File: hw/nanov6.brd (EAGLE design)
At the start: 34.9 x 35.2 mm, 28 parts, among them CON1 503548-1220, J1 M08X2, Q4 BSS138, U1 TPS622XX

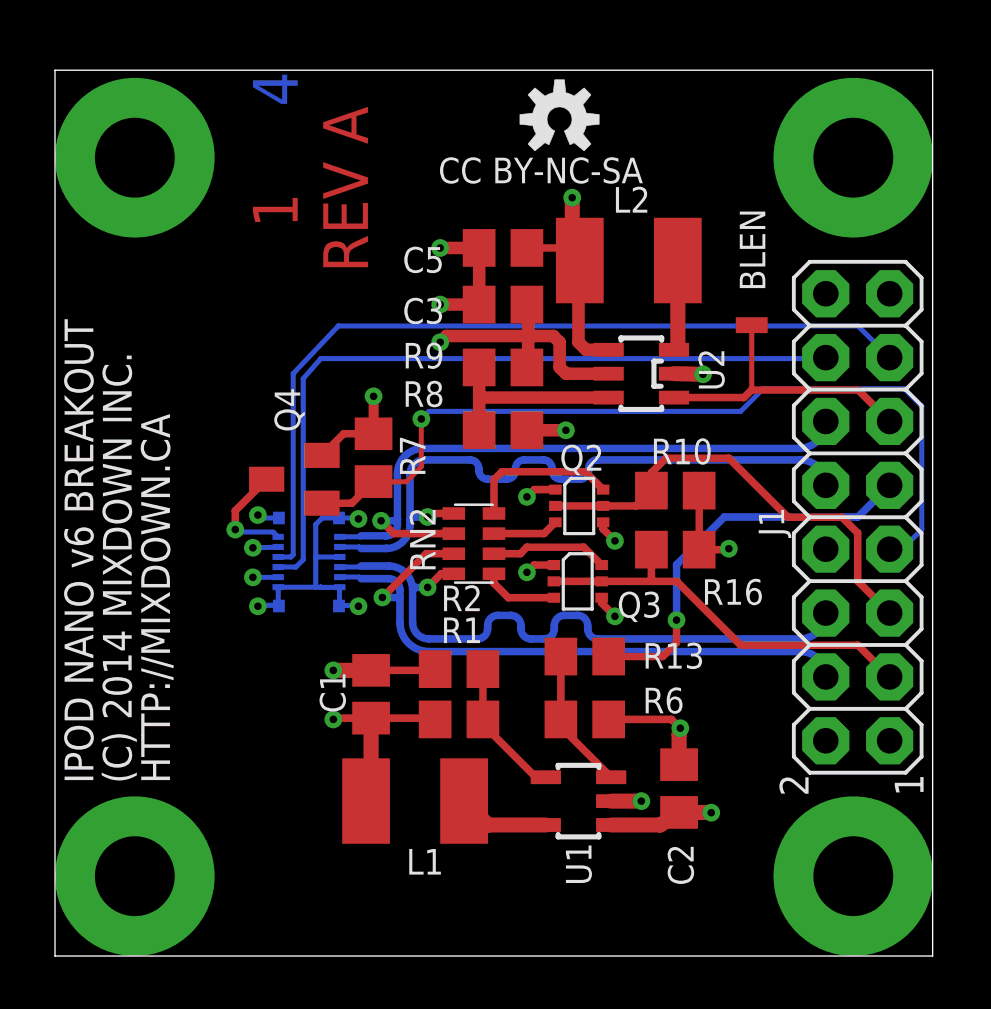
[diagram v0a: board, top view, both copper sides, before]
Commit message: add pulldown to RST#, make 3.3VEN active-high. Resolves #471, refs #469.
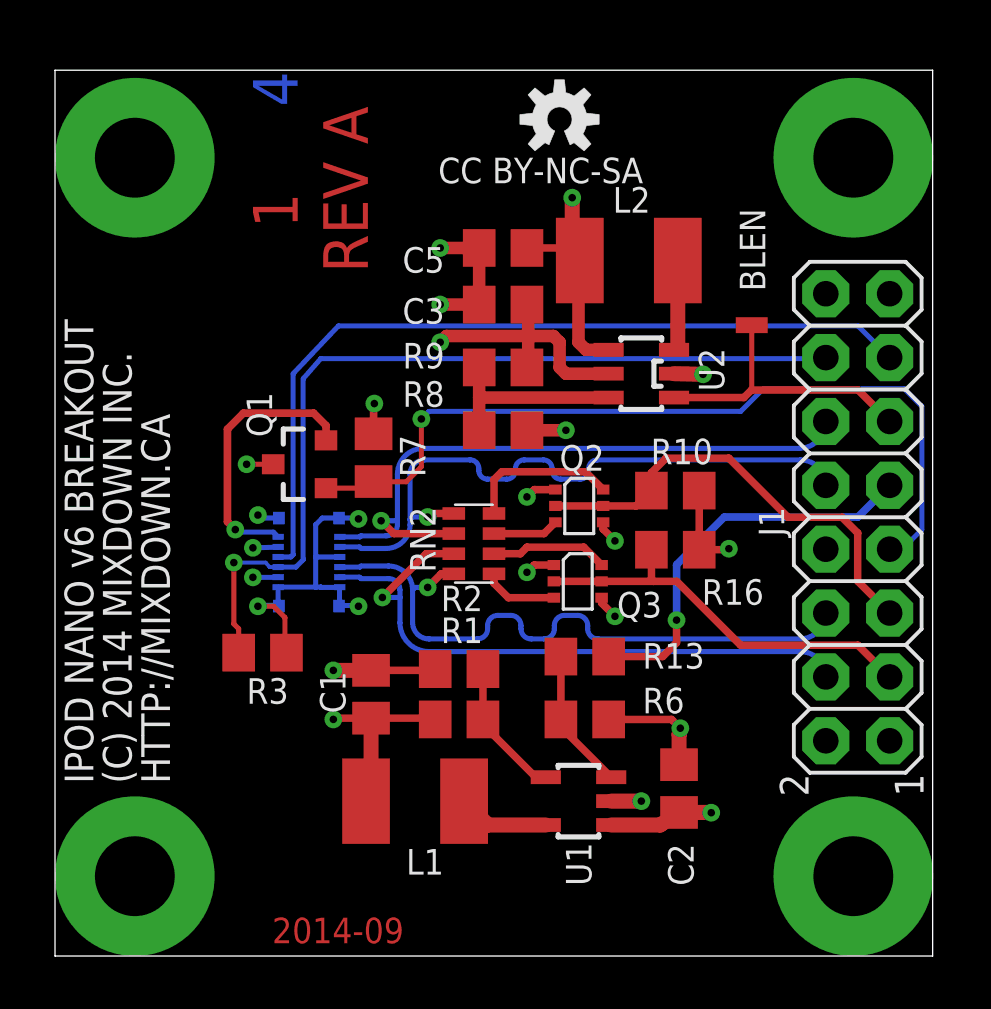
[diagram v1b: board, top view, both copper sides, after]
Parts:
- removed Q4: BSS138, SparkFun:SOT23
- added Q1: BSS84, SparkFun:SOT23-3
- added R3: 1k, rcl:R0805
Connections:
- net +3.3: now also Q1.3; no longer Q4.2, R7.2
- net 3.3VEN: now also Q1.1; no longer Q4.1
- net 3.3_SW: now also Q1.2; no longer Q4.3
- net GND: now also R3.2, R7.2
- net RST#: now also R3.1
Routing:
- net 3.3_SW: track 4.34 -> 10.9 mm
- net RST#: track 29.5 -> 35.0 mm, vias 0 -> 1
- net GND: track 37.4 -> 41.3 mm, vias 16 -> 17
- net +3.3: track 19.1 -> 16.2 mm
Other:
- board text added: "2014-09"

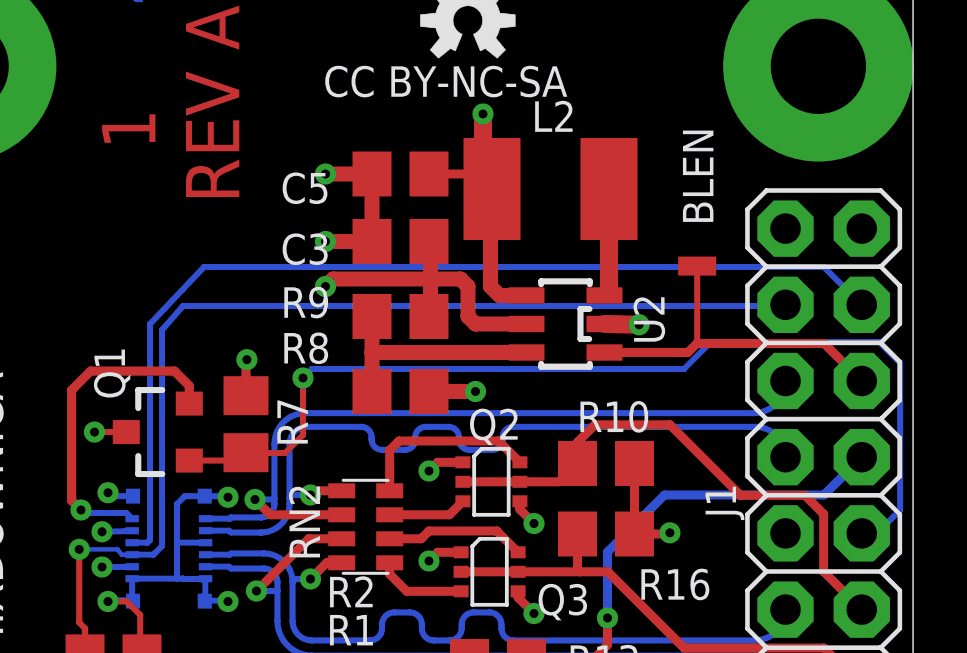
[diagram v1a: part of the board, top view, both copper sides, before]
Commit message: add pulldown to BLEN. Resolves #469.
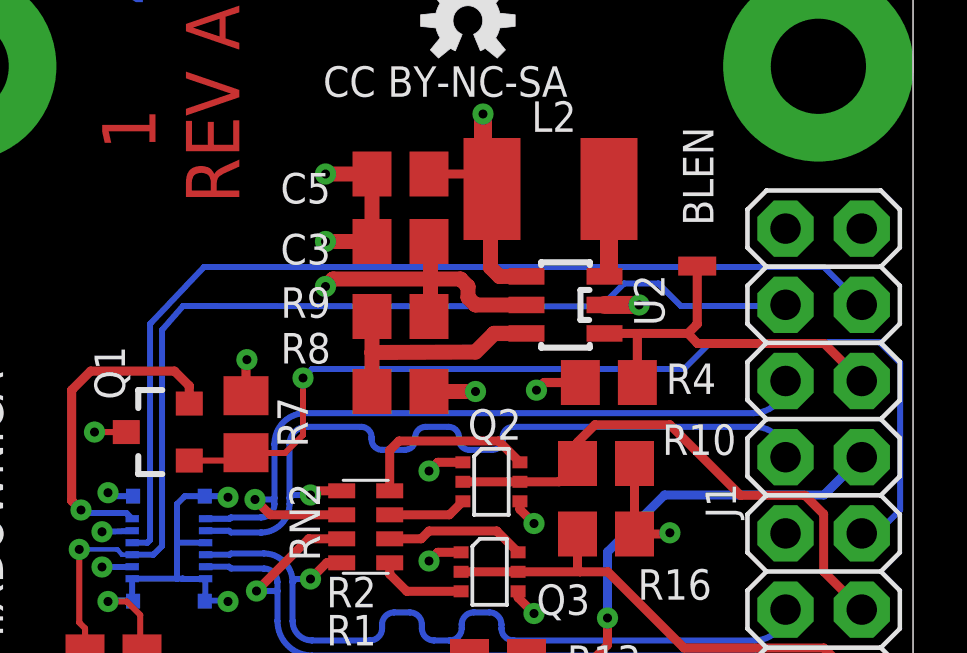
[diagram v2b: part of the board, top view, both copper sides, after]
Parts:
- added R4: 1k, rcl:R0805
- moved U2 0.64 mm to (23.3, 23.8)
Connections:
- net BL: now also R4.1
- net GND: now also R4.2
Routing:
- net GND: track 41.3 -> 42.9 mm, vias 17 -> 18
- net BL: track 11.8 -> 13.3 mm
- net N$7: track 3.61 -> 2.98 mm
- net LED+: track 26.3 -> 25.7 mm
- net +3.3: track 16.2 -> 15.6 mm
- net RST#: track 35.0 -> 35.6 mm
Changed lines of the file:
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@@
 <setting verticaltext="up"/>
 </settings>
-<grid distance="25" unitdist="mil" unit="mil" style="lines" multiple="1" display="yes" altdistance="0.025" altunitdist="inch" altunit="inch"/>
+<grid distance="5" unitdist="mil" unit="mil" style="lines" multiple="1" display="yes" altdistance="0.025" altunitdist="inch" altunit="inch"/>
 <layers>
 <layer number="1" name="Top" color="4" fill="1" visible="yes" active="yes"/>
@@
 <layer number="37" name="tTest" color="7" fill="1" visible="no" active="yes"/>
 <layer number="38" name="bTest" color="7" fill="1" visible="no" active="yes"/>
-<layer number="39" name="tKeepout" color="4" fill="11" visible="no" active="yes"/>
+<layer number="39" name="tKeepout" color="4" fill="11" visible="yes" active="yes"/>
 <layer number="40" name="bKeepout" color="1" fill="11" visible="yes" active="yes"/>
 <layer number="41" name="tRestrict" color="4" fill="10" visible="yes" active="yes"/>
@@
 </element>
 <element name="R10" library="rcl" package="R0805" value="1k" x="24.67" y="18.51" smashed="yes" rot="R180">
-<attribute name="NAME" x="26.162" y="20.574" size="1.016" layer="25" ratio="10" rot="R180"/>
+<attribute name="NAME" x="26.543" y="18.796" size="1.016" layer="25" ratio="10"/>
 <attribute name="VALUE" x="25.305" y="21.05" size="1.27" layer="27" rot="R180"/>
 </element>
@@
 <attribute name="VALUE" x="15.21" y="19.185" size="1.27" layer="27" rot="R90"/>
 </element>
-<element name="U2" library="ak-misc" package="SOT23-6" value="" x="23.32" y="23.16" smashed="yes" rot="R90">
-<attribute name="NAME" x="26.622" y="22.4615" size="1.016" layer="25" ratio="10" rot="R90"/>
-<attribute name="VALUE" x="23.5105" y="22.2075" size="0.4064" layer="27" rot="R90"/>
+<element name="U2" library="ak-misc" package="SOT23-6" value="" x="23.32" y="23.795" smashed="yes" rot="R90">
+<attribute name="NAME" x="26.622" y="23.0965" size="1.016" layer="25" ratio="10" rot="R90"/>
+<attribute name="VALUE" x="23.5105" y="22.8425" size="0.4064" layer="27" rot="R90"/>
 </element>
 <element name="R8" library="rcl" package="R0805" value="TBD" x="17.82" y="20.91" smashed="yes">
@@
 <attribute name="NAME" x="7.62" y="10.033" size="1.016" layer="25" ratio="10"/>
 <attribute name="VALUE" x="7.62" y="9.525" size="1.27" layer="27"/>
+</element>
+<element name="R4" library="rcl" package="R0805" value="1k" x="24.765" y="21.209" smashed="yes" rot="R180">
+<attribute name="NAME" x="26.67" y="20.828" size="1.016" layer="25" ratio="10"/>
+<attribute name="VALUE" x="25.4" y="23.749" size="1.27" layer="27" rot="R180"/>
 </element>
 </elements>
@@
 <wire x1="22.1201" y1="6.16" x2="23.32" y2="6.16" width="0.6" layer="1"/>
 <via x="23.32" y="6.16" extent="1-16" drill="0.3" diameter="0.3"/>
-<wire x1="24.6201" y1="23.16" x2="25.7732" y2="23.1346" width="0.6" layer="1"/>
-<via x="25.7732" y="23.1346" extent="1-16" drill="0.3" diameter="0.3"/>
+<wire x1="24.6201" y1="23.795" x2="25.7732" y2="23.795" width="0.6" layer="1"/>
+<via x="25.7732" y="23.795" extent="1-16" drill="0.3" diameter="0.3"/>
 <wire x1="16.87" y1="28.16" x2="15.32" y2="28.16" width="0.5" layer="1"/>
 <via x="15.32" y="28.16" extent="1-16" drill="0.3" diameter="0.3"/>
@@
 <wire x1="9.144" y1="13.462" x2="8.696" y2="13.91" width="0.2032" layer="1"/>
 <wire x1="8.696" y1="13.91" x2="8.07" y2="13.91" width="0.2032" layer="1"/>
+<contactref element="R4" pad="2"/>
+<wire x1="23.815" y1="21.209" x2="22.606" y2="21.209" width="0.3048" layer="1"/>
+<wire x1="22.606" y1="21.209" x2="22.352" y2="20.955" width="0.3048" layer="1"/>
+<via x="22.352" y="20.955" extent="1-16" drill="0.3"/>
 </signal>
 <signal name="CLKLOW">
@@
 <wire x1="9.8716" y1="15.76" x2="9.8716" y2="22.96" width="0.2" layer="16"/>
 <wire x1="9.8716" y1="22.96" x2="10.57" y2="23.76" width="0.2" layer="16"/>
-<wire x1="10.57" y1="23.76" x2="30.615" y2="23.76" width="0.2" layer="16"/>
+<wire x1="10.57" y1="23.76" x2="24.511" y2="23.749" width="0.2" layer="16"/>
+<wire x1="24.511" y1="23.749" x2="25.273" y2="24.511" width="0.2" layer="16"/>
+<wire x1="25.273" y1="24.511" x2="26.416" y2="24.511" width="0.2" layer="16"/>
+<wire x1="26.416" y1="24.511" x2="27.167" y2="23.76" width="0.2" layer="16"/>
+<wire x1="27.167" y1="23.76" x2="30.615" y2="23.76" width="0.2" layer="16"/>
 <wire x1="30.615" y1="23.76" x2="30.655" y2="23.8" width="0.2" layer="16"/>
 <contactref element="R3" pad="1"/>
@@
 <contactref element="C3" pad="1"/>
 <contactref element="R9" pad="1"/>
-<wire x1="22.0199" y1="23.16" x2="20.32" y2="23.16" width="0.5" layer="1"/>
-<wire x1="20.32" y1="23.16" x2="20.07" y2="23.41" width="0.5" layer="1"/>
-<wire x1="20.07" y1="23.41" x2="20.07" y2="24.41" width="0.5" layer="1"/>
+<wire x1="22.0199" y1="23.795" x2="20.32" y2="23.795" width="0.5" layer="1"/>
+<wire x1="20.32" y1="23.795" x2="20.07" y2="24.045" width="0.5" layer="1"/>
+<wire x1="20.07" y1="24.045" x2="20.07" y2="24.41" width="0.5" layer="1"/>
 <wire x1="20.07" y1="24.41" x2="19.82" y2="24.66" width="0.5" layer="1"/>
 <wire x1="18.82" y1="23.46" x2="18.77" y2="23.41" width="0.5" layer="1"/>
@@
 <wire x1="22.1201" y1="5.21" x2="24.07" y2="5.21" width="0.6" layer="1"/>
 <wire x1="24.07" y1="5.21" x2="24.82" y2="5.71" width="0.6" layer="1"/>
-<wire x1="22.0199" y1="24.11" x2="21.12" y2="24.11" width="0.5" layer="1"/>
-<wire x1="21.12" y1="24.11" x2="20.82" y2="24.41" width="0.5" layer="1"/>
-<wire x1="20.82" y1="24.41" x2="20.82" y2="27.11" width="0.5" layer="1"/>
+<wire x1="22.0199" y1="24.745" x2="21.12" y2="24.745" width="0.5" layer="1"/>
+<wire x1="21.12" y1="24.745" x2="20.82" y2="25.045" width="0.5" layer="1"/>
+<wire x1="20.82" y1="25.045" x2="20.82" y2="27.11" width="0.5" layer="1"/>
 <wire x1="20.82" y1="27.11" x2="20.87" y2="27.66" width="0.3" layer="1"/>
 <wire x1="20.57" y1="28.16" x2="21.07" y2="27.66" width="0.5" layer="1"/>
@@
 <contactref element="U2" pad="1"/>
 <contactref element="L2" pad="2"/>
-<wire x1="24.6201" y1="24.11" x2="24.77" y2="24.2599" width="0.2032" layer="1"/>
-<wire x1="24.77" y1="24.2599" x2="24.77" y2="27.66" width="0.6" layer="1"/>
+<wire x1="24.6201" y1="24.745" x2="24.77" y2="24.8949" width="0.2032" layer="1"/>
+<wire x1="24.77" y1="24.8949" x2="24.77" y2="27.66" width="0.6" layer="1"/>
 </signal>
 <signal name="N$13">
@@
 <contactref element="R9" pad="2"/>
 <contactref element="U2" pad="4"/>
-<wire x1="22.0199" y1="22.21" x2="16.87" y2="22.21" width="0.5" layer="1"/>
+<wire x1="20.32" y1="22.225" x2="16.87" y2="22.21" width="0.5" layer="1"/>
 <wire x1="16.87" y1="22.21" x2="16.87" y2="20.91" width="0.5" layer="1"/>
 <wire x1="16.87" y1="23.41" x2="16.87" y2="22.21" width="0.5" layer="1"/>
+<wire x1="22.0199" y1="22.845" x2="20.94" y2="22.845" width="0.508" layer="1"/>
+<wire x1="20.94" y1="22.845" x2="20.32" y2="22.225" width="0.508" layer="1"/>
 </signal>
 <signal name="BL">
@@
 <wire x1="33.195" y1="21.26" x2="31.945" y2="22.51" width="0.3" layer="1"/>
 <wire x1="31.945" y1="22.51" x2="27.72" y2="22.51" width="0.3" layer="1"/>
-<wire x1="27.4" y1="22.21" x2="24.6201" y2="22.21" width="0.3" layer="1"/>
-<wire x1="27.71" y1="25.09" x2="27.71" y2="22.52" width="0.2032" layer="1"/>
+<wire x1="27.4" y1="22.845" x2="25.781" y2="22.845" width="0.3" layer="1"/>
+<wire x1="25.781" y1="22.845" x2="24.6201" y2="22.845" width="0.3" layer="1"/>
 <wire x1="27.72" y1="22.51" x2="27.71" y2="22.52" width="0.3" layer="1"/>
-<wire x1="27.71" y1="22.52" x2="27.4" y2="22.21" width="0.3" layer="1"/>
+<wire x1="27.71" y1="22.52" x2="27.4" y2="22.845" width="0.3" layer="1"/>
+<contactref element="R4" pad="1"/>
+<wire x1="27.71" y1="25.09" x2="27.71" y2="23.155" width="0.3048" layer="1"/>
+<wire x1="27.71" y1="23.155" x2="27.4" y2="22.845" width="0.3048" layer="1"/>
+<wire x1="25.715" y1="21.209" x2="25.715" y2="22.779" width="0.3048" layer="1"/>
+<wire x1="25.715" y1="22.779" x2="25.781" y2="22.845" width="0.3048" layer="1"/>
 </signal>
 </signals>
